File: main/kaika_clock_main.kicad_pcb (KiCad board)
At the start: 2 copper layers, 128 x 32 mm, 58 parts, among them J1 Conn_01x04, J6 Conn_01x05, P1 MICRO-USB_SMD, Q1 Q_NPN_BEC, SW1 TC-1102N-C-QL-B, SW2 SW-1101-B-W, SW3 TC-1102N-C-QL-B, U1 AMS1117-3.3, U2 STM32F103C8Tx, U3 DS3231MZ, U4 DHT11_OR_22, Y1 Crystal

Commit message: modify the main pcb
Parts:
- moved C12 6.18 mm to (160.6, 124.0)
- moved C11 6.06 mm to (152.6, 124.0)
- moved R4 5.34 mm to (156.6, 124.1)
- moved Y1 3.16 mm to (156.6, 128.5)
- moved C10 0.09 mm to (212.2, 126.0)
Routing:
- net OSC_IN: track 24.6 -> 14.7 mm
- net GND: track 448.3 -> 458.1 mm, vias 42 -> 43
- net OSC_OUT: track 24.1 -> 14.4 mm
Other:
- net class Vcc added: clearance 0.2, trace_width 0.5, via_dia 1, via_drill 0.5

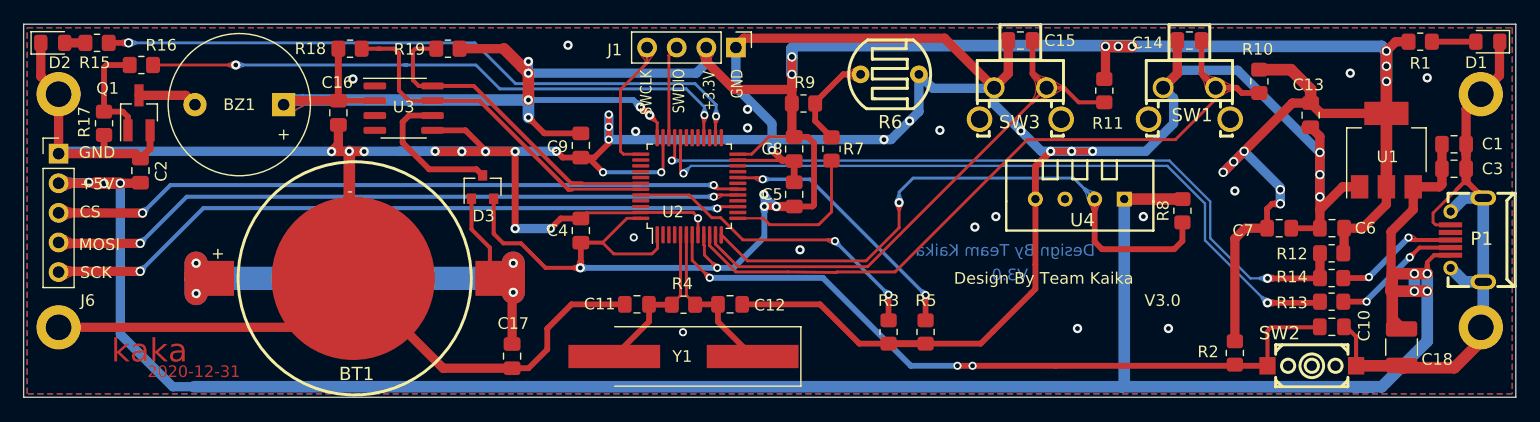
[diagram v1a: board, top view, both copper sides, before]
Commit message: modify the jumper
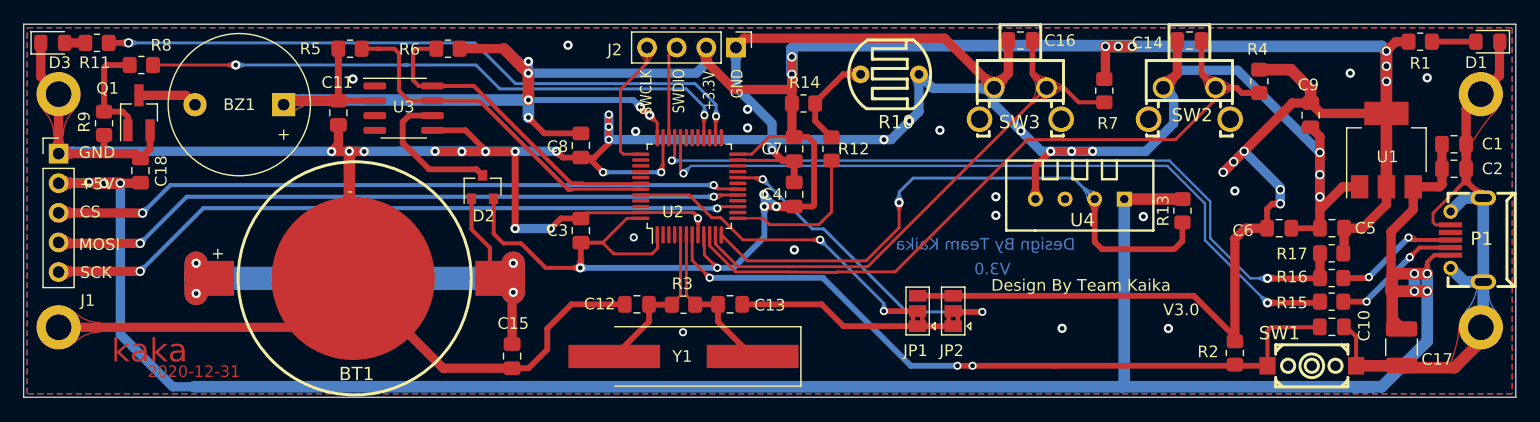
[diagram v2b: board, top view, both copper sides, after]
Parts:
- removed the R3 at (174.2, 126.4)
- removed the R5 at (177.4, 126.4)
- added JP1: Jumper_NC_Dual, Jumper:SolderJumper-3_P1.3mm_Bridged2Bar12_Pad1.0x1.5mm, F.Cu at (176.7, 124.6)
- added JP2: Jumper_NC_Dual, Jumper:SolderJumper-3_P1.3mm_Bridged2Bar12_Pad1.0x1.5mm, F.Cu at (179.7, 124.6)
- renumbered C16 to C11, C11 to C12, C12 to C13, C17 to C15, C15 to C16, C18 to C17, C2 to C18, C3 to C2, C4 to C3, C5 to C4, C6 to C5, C7 to C6, C8 to C7, C9 to C8, C13 to C9, D3 to D2, D2 to D3, J6 to J1, J1 to J2, R6 to R10, R15 to R11, R7 to R12, R8 to R13, R9 to R14, R13 to R15, R14 to R16, R12 to R17, R4 to R3, R10 to R4, R18 to R5, R19 to R6, R11 to R7, R16 to R8, R17 to R9, SW2 to SW1, SW1 to SW2
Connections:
- P1 pad 4: Net-(P1-Pad4) -> (no net)
- SW2 pad 3: Net-(SW1-Pad3) -> (no net)
- SW2 pad 4: Net-(SW1-Pad4) -> (no net)
- SW3 pad 3: Net-(SW3-Pad3) -> (no net)
- SW3 pad 4: Net-(SW3-Pad4) -> (no net)
- U2 pad 14: Net-(U2-Pad14) -> (no net)
- U2 pad 16: Net-(U2-Pad16) -> (no net)
- U2 pad 19: Net-(U2-Pad19) -> (no net)
- U2 pad 2: Net-(U2-Pad2) -> (no net)
- U2 pad 21: Net-(U2-Pad21) -> (no net)
- U2 pad 22: Net-(U2-Pad22) -> (no net)
- U2 pad 25: Net-(U2-Pad25) -> (no net)
- U2 pad 27: Net-(U2-Pad27) -> (no net)
- U2 pad 29: Net-(U2-Pad29) -> (no net)
- U2 pad 3: Net-(U2-Pad3) -> (no net)
- U2 pad 30: Net-(U2-Pad30) -> (no net)
- U2 pad 31: Net-(U2-Pad31) -> (no net)
- U2 pad 38: Net-(U2-Pad38) -> (no net)
- U2 pad 39: Net-(U2-Pad39) -> (no net)
- U2 pad 4: Net-(U2-Pad4) -> (no net)
- U2 pad 40: Net-(U2-Pad40) -> (no net)
- U2 pad 41: Net-(U2-Pad41) -> (no net)
- U2 pad 45: Net-(U2-Pad45) -> (no net)
- U2 pad 46: Net-(U2-Pad46) -> (no net)
- U3 pad 1: Net-(U3-Pad1) -> (no net)
- U3 pad 3: Net-(U3-Pad3) -> (no net)
- U3 pad 4: Net-(U3-Pad4) -> (no net)
- U4 pad 3: Net-(U4-Pad3) -> (no net)
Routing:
- net +3V3: track 300.5 -> 329.9 mm
- net GND: track 458.1 -> 440.8 mm
- net BOOT1: track 22.5 -> 28.3 mm
- net BOOT0: track 27.1 -> 28.3 mm

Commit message: modify the main
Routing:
- net VCC: track 201.7 -> 202.2 mm

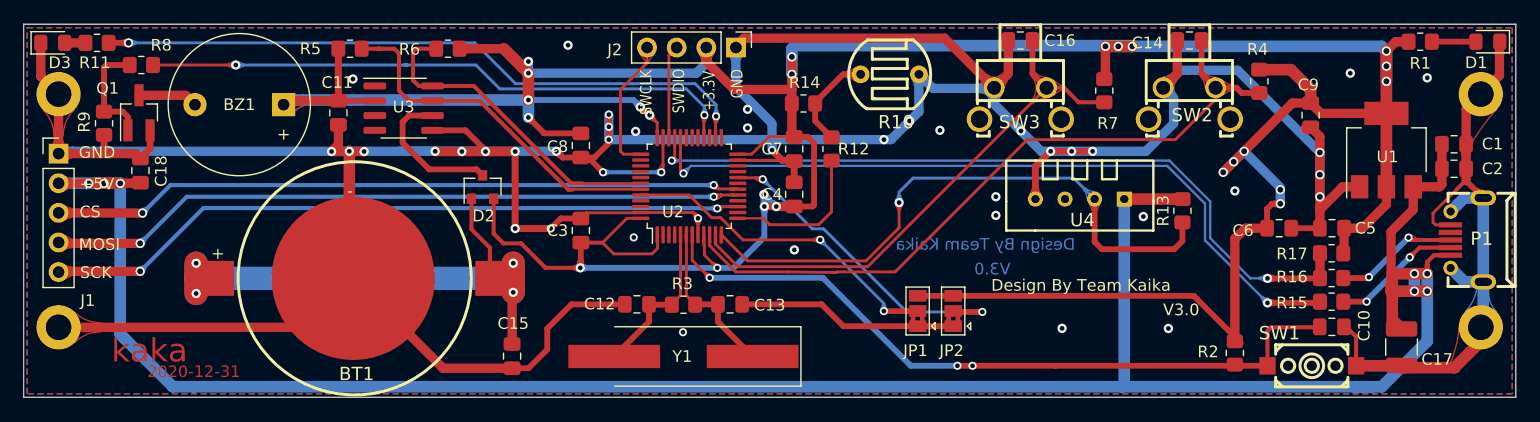
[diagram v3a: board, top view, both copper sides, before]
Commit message: modify change usb to typc-c
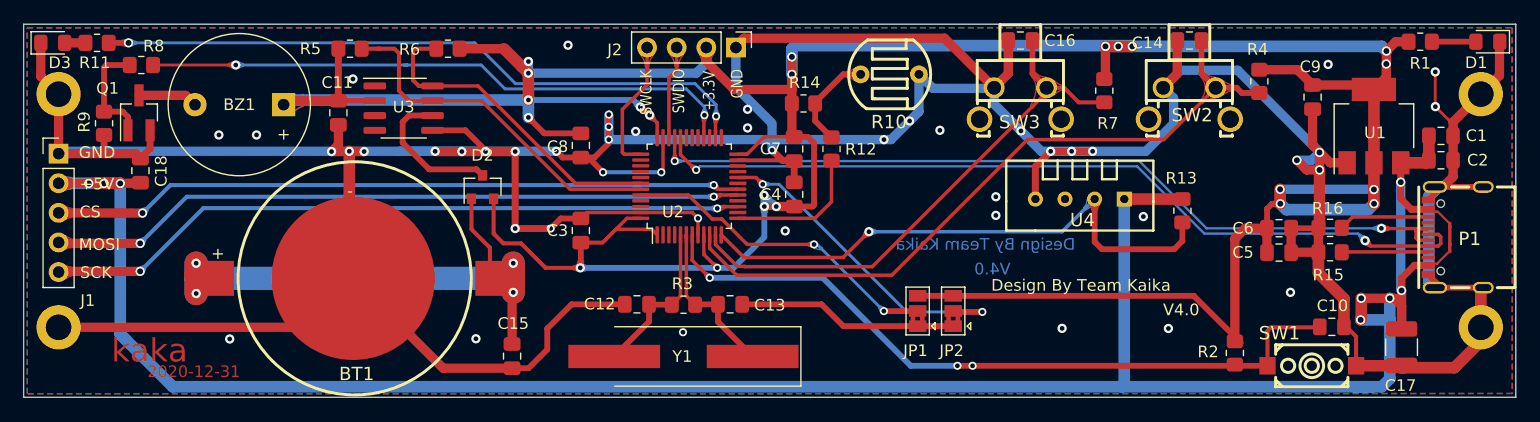
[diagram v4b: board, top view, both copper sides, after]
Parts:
- removed R17: 1.5K, Resistor_SMD:R_0805_2012Metric_Pad1.20x1.40mm_HandSolder
- P1: value MICRO-USB_SMD -> USB-C-SMD_TYPE-C16PIN_C393939; footprint Kaka-footprints:MICRO-USB-SMD_MICRO-USB-18 -> Kaka-footprints:USB-C-SMD_TYPE-C16PIN_C393939
- R15, R16: value 33 -> 5.1K
- Y1: value Crystal -> 8MHZ
- moved C5 5.00 mm to (207.7, 119.6), turned to 0 degrees
- moved R16 4.31 mm to (212.1, 117.5)
- moved R15 4.24 mm to (212.1, 119.6)
- moved U1 2.32 mm to (215.8, 108.7)
- moved C9 1.56 mm to (210.6, 106.2)
- moved C2 1.34 mm to (221.6, 111.7)
- moved C1 1.33 mm to (221.6, 109.6)
- moved P1 0.98 mm to (222.8, 118.3)
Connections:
- P1 pad 1: VCC -> GND
- P1 pad 2: Net-(P1-Pad2) -> GND
- P1 pad 3: Net-(P1-Pad3) -> GND
- P1 pad 4: (no net) -> GND
- R15 pad 1: Net-(P1-Pad2) -> Net-(P1-PadA5)
- R15 pad 2: USB_D- -> GND
- R16 pad 1: Net-(P1-Pad3) -> Net-(P1-PadB5)
- R16 pad 2: USB_D+ -> GND
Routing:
- net GND: track 440.8 -> 460.0 mm, vias 43 -> 47
- net +3V3: track 329.9 -> 318.0 mm, vias 24 -> 22
- net Net-(P1-Pad2): track 11.2 -> 0.00 mm, vias 2 -> 0
- net Net-(P1-Pad3): track 10.7 -> 0.00 mm, vias 2 -> 0
- net VCC: track 202.2 -> 211.9 mm, vias 7 -> 8
- net USB_D-: track 64.7 -> 72.8 mm
- net Net-(P1-PadB5): track 0.00 -> 7.81 mm
- net Net-(P1-PadA5): track 0.00 -> 7.43 mm
- net USB_D+: track 65.9 -> 71.9 mm
- net TEMP_SENSOR: track 52.4 -> 48.9 mm
- net LIGHT_SENSOR: track 13.2 -> 12.2 mm
- net I2C1_SCL: track 29.3 -> 28.4 mm
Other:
- board text added: "Design By Team Kaika V4.0"
- board text added: "V4.0"
- board text removed: "Design By Team Kaika V3.0"
- board text removed: "V3.0"

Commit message: modify main
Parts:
- moved C17 0.10 mm to (218.2, 127.8)
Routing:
- net +3V3: track 318.0 -> 321.1 mm
- net VCC: track 211.9 -> 209.1 mm
- net RESET: vias 3 -> 2
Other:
- board text added: "Design By Team Kaika V4.5"
- board text added: "V4.5"
- board text removed: "Design By Team Kaika V4.0"
- board text removed: "V4.0"

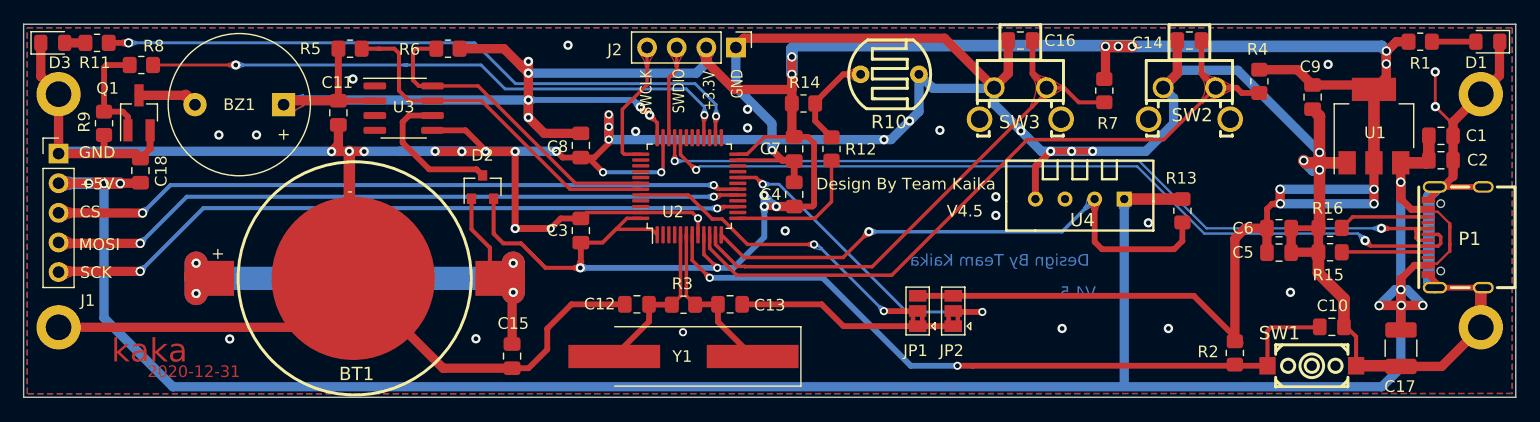
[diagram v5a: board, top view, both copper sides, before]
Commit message: modify the main and display
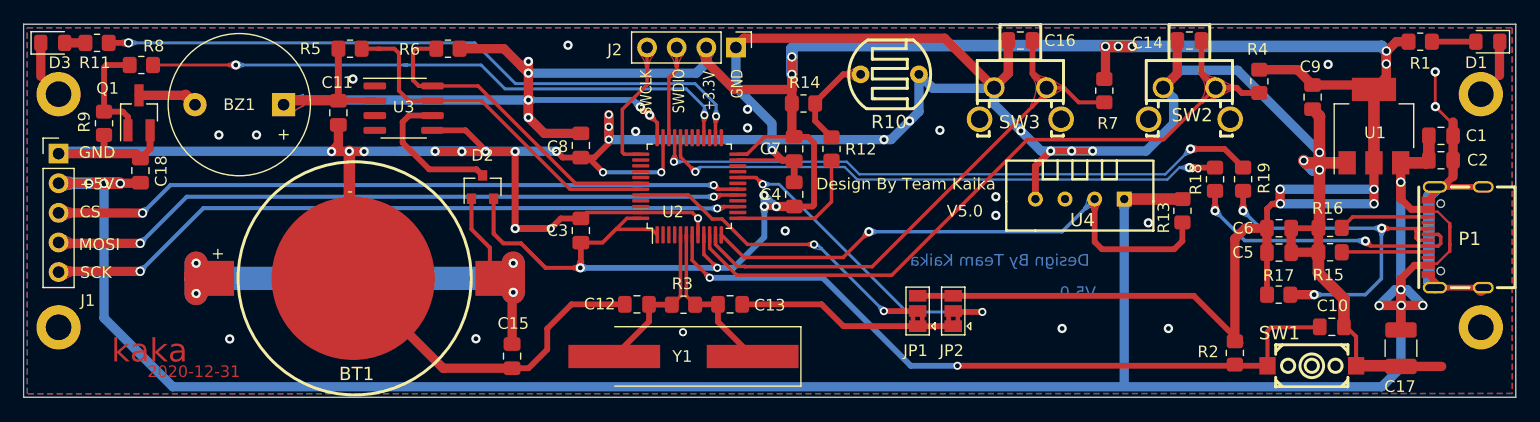
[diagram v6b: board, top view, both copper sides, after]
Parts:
- added R17: 1.5K, Resistor_SMD:R_0805_2012Metric_Pad1.20x1.40mm_HandSolder, F.Cu at (207.7, 123.2)
- added R18: 33, Resistor_SMD:R_0805_2012Metric_Pad1.20x1.40mm_HandSolder, F.Cu at (202.2, 113.3)
- added R19: 33, Resistor_SMD:R_0805_2012Metric_Pad1.20x1.40mm_HandSolder, F.Cu at (204.6, 113.3)
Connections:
- P1 pad A6: USB_D+ -> Net-(P1-PadA6)
- P1 pad A7: USB_D- -> Net-(P1-PadA7)
- P1 pad B6: USB_D+ -> Net-(P1-PadA6)
- P1 pad B7: USB_D- -> Net-(P1-PadA7)
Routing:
- net GND: track 460.0 -> 416.6 mm, vias 47 -> 46
- net Net-(P1-PadA6): track 0.00 -> 33.9 mm, vias 0 -> 3
- net Net-(P1-PadA7): track 0.00 -> 24.4 mm, vias 0 -> 2
- net USB_D-: track 72.8 -> 49.8 mm
- net USB_D+: track 71.9 -> 52.9 mm
- net +3V3: track 321.1 -> 324.8 mm
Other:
- board text added: "Design By Team Kaika V5.0"
- board text added: "V5.0"
- board text removed: "Design By Team Kaika V4.5"
- board text removed: "V4.5"

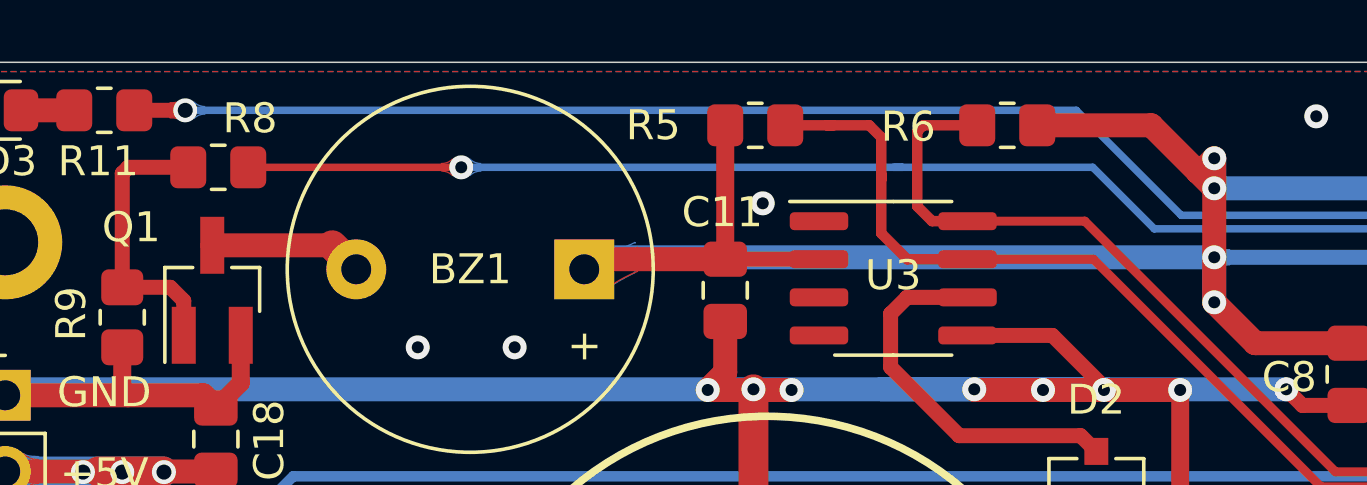
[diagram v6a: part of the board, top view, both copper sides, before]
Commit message: modify the display
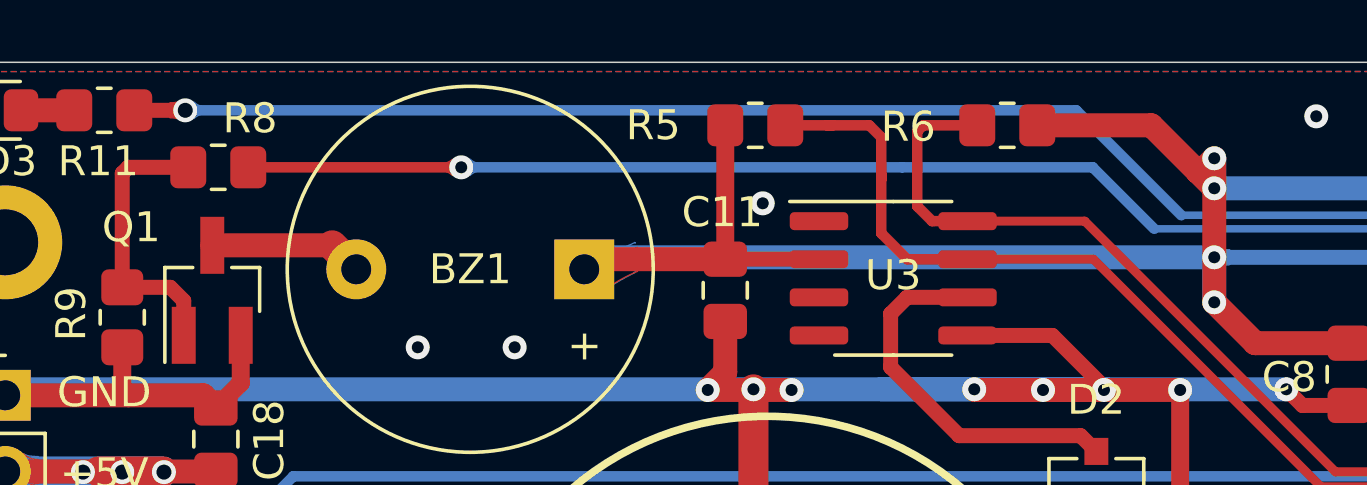
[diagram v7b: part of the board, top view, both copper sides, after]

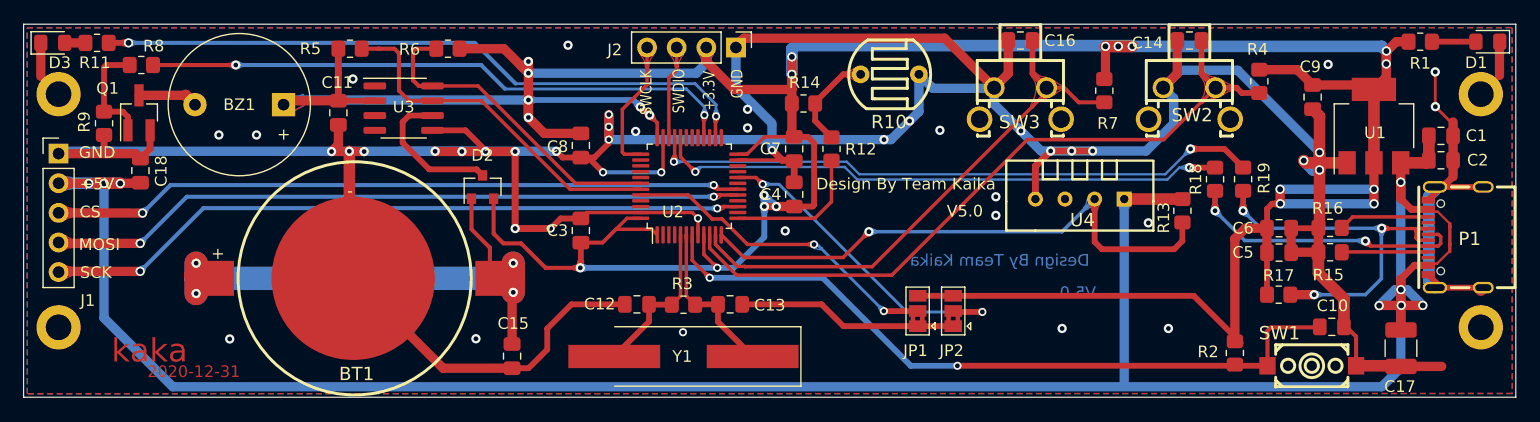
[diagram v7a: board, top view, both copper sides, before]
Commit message: modify main and display
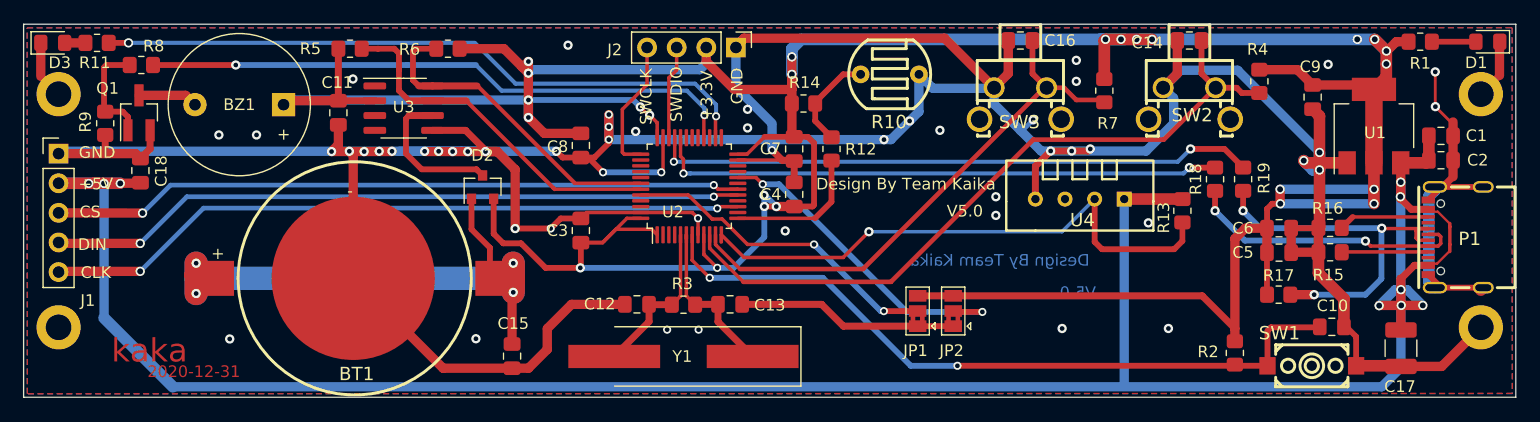
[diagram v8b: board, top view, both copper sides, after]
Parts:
- moved R9 0.10 mm to (107.0, 108.5)
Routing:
- net GND: track 416.6 -> 431.2 mm, vias 46 -> 52
- net +3V3: track 324.8 -> 329.4 mm, vias 22 -> 25
- net USB_D+: track 52.9 -> 52.1 mm
- net USB_D-: track 49.8 -> 49.2 mm
- net VCC: vias 8 -> 9
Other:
- board text added: "CLK"
- board text added: "DIN"
- board text removed: "MOSI"
- board text removed: "SCK"
